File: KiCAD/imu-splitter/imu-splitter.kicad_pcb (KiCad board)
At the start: 2 copper layers, 54 x 54 mm, 16 parts, among them J1 4P4C, J2 4P4C, J3 4P4C, J4 4P4C, J5 4P4C, J6 4P4C, J7 SHF-113-01-L-D-SM, J8 Conn_01x04, J9 Conn_01x05, U1 AZ1117-3.3

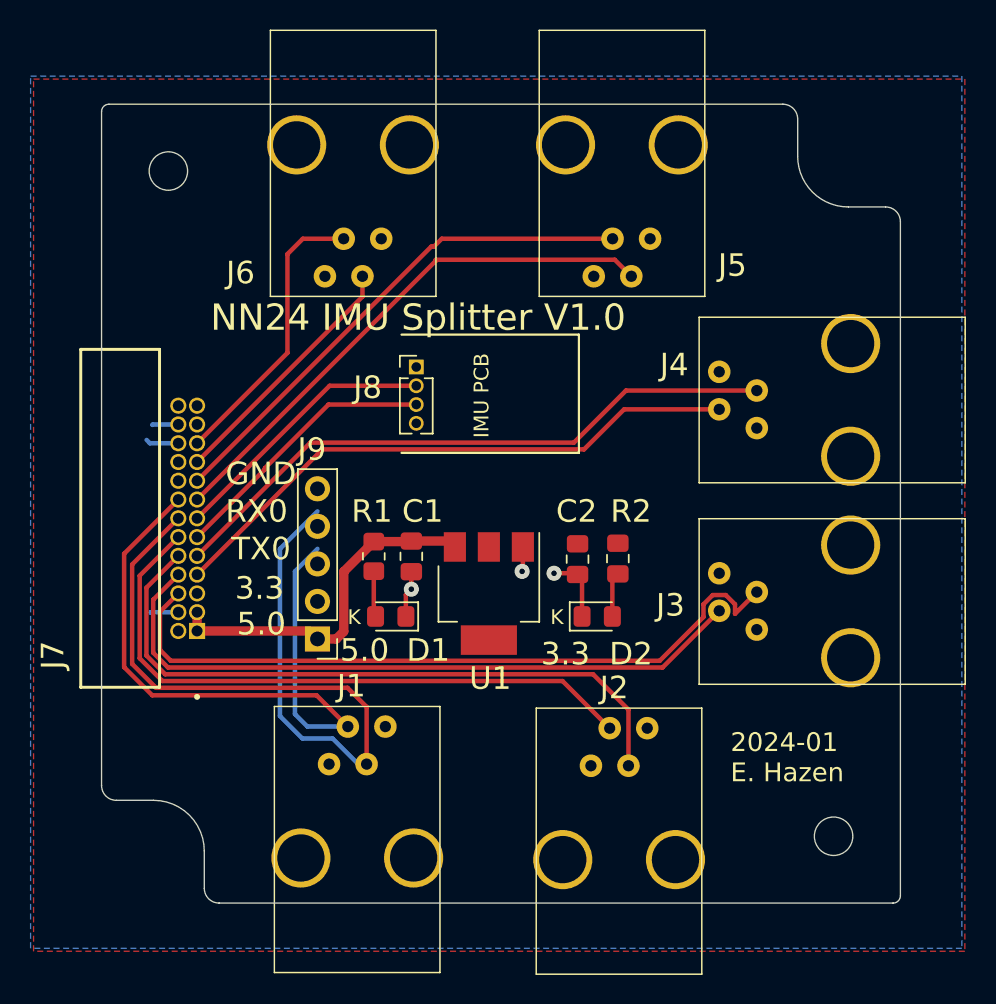
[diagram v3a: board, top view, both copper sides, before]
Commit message: Update splitter to V2.0
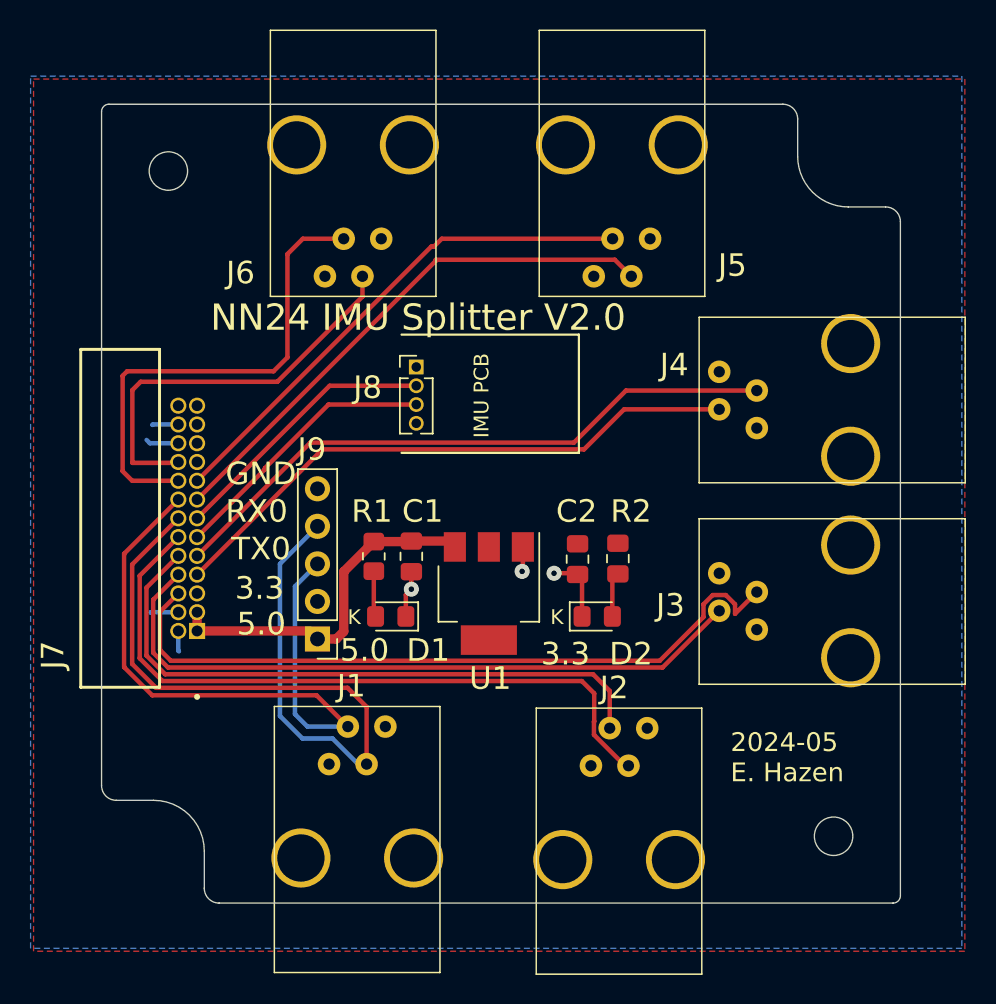
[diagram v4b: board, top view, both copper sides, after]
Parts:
- J7: value SHF-113-01-L-D-SM -> 3220-26-0200-00
- U1: value AZ1117-3.3 -> AP2114H-3.3TRG1
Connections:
- J2 pad 2: /RX1 -> /TX1
- J2 pad 3: /TX1 -> /RX1
- J7 pad 18: unconnected-(J7-Pin_18-Pad18) -> /RX5
- J7 pad 19: /TX5 -> unconnected-(J7-Pin_19-Pad19)
- J7 pad 20: unconnected-(J7-Pin_20-Pad20) -> /TX5
- J7 pad 21: /RX5 -> unconnected-(J7-Pin_21-Pad21)
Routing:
- net /RX5: track 19.6 -> 33.4 mm
- net /TX5: track 17.2 -> 27.6 mm
- net /RX1: track 43.0 -> 47.0 mm
- net /TX1: track 45.6 -> 42.5 mm
- net GND: track 15.4 -> 16.8 mm
- net /TX0: track 45.4 -> 44.4 mm
- net /RX0: track 54.2 -> 53.2 mm
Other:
- board text added: "2024-05 E. Hazen"
- board text added: "NN24 IMU Splitter V2.0"
- board text removed: "2024-01 E. Hazen"
- board text removed: "NN24 IMU Splitter V1.0"

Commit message: working on 3D of box
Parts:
- added N1: 1551T, models:1551T, F.Cu at (168.3, 79.4)
- added N2: 1551T_lid, models:1551T_lid, F.Cu at (168.3, 79.4)

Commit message: Candidate V2 layout
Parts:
- removed N1: 1551T, models:1551T
- removed N2: 1551T_lid, models:1551T_lid
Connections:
- J7 pad 11: /RX6 -> /TX6
- J7 pad 13: /TX6 -> /RX6
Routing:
- net /RX6: track 18.6 -> 18.0 mm, vias 0 -> 1
- net /TX6: track 18.5 -> 19.1 mm
